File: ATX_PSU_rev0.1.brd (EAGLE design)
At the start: 160 x 100 mm, 60 parts, among them J1 ATX24RH, U1 INA169, U2 INA169, U3 INA169, U4 INA169, U5 INA169

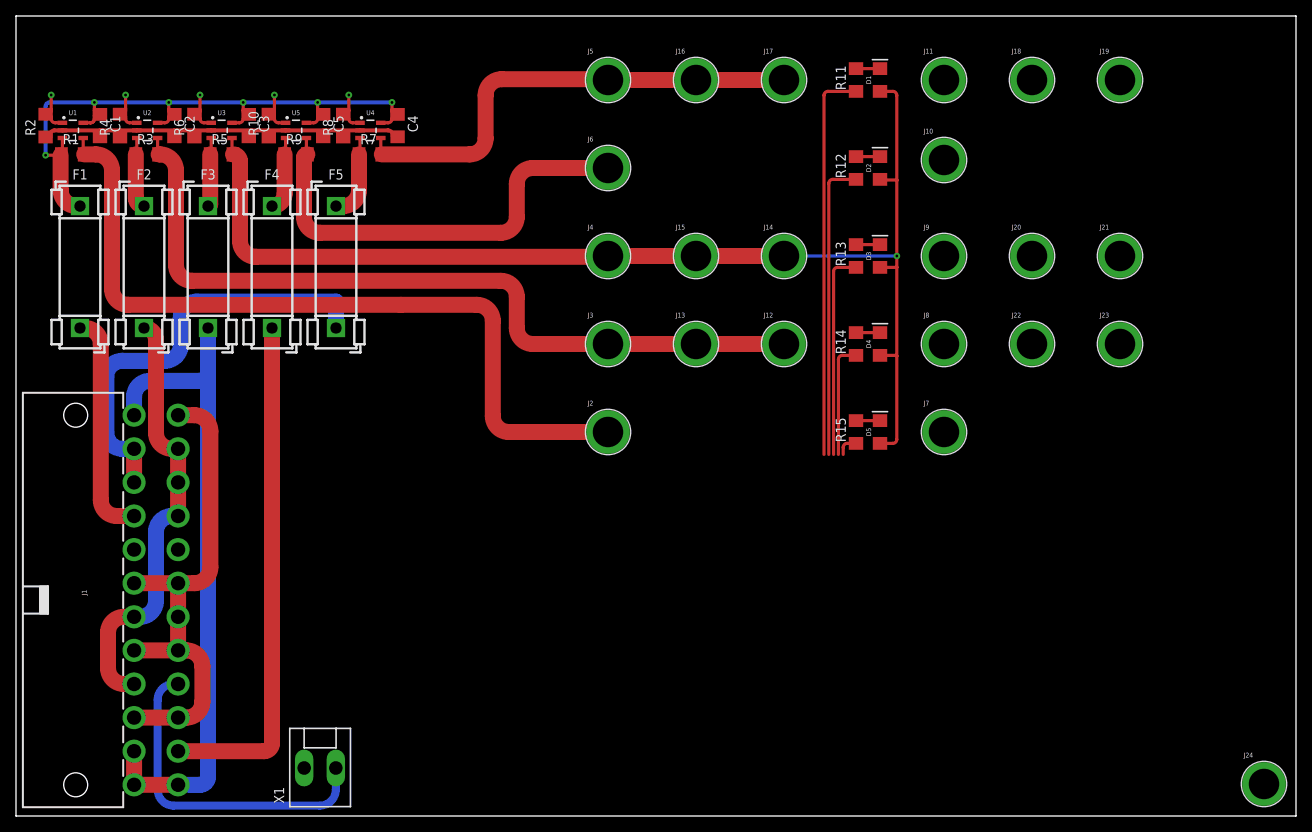
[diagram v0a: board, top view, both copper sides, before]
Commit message: added microcontroller
made some connections to microcontroller.
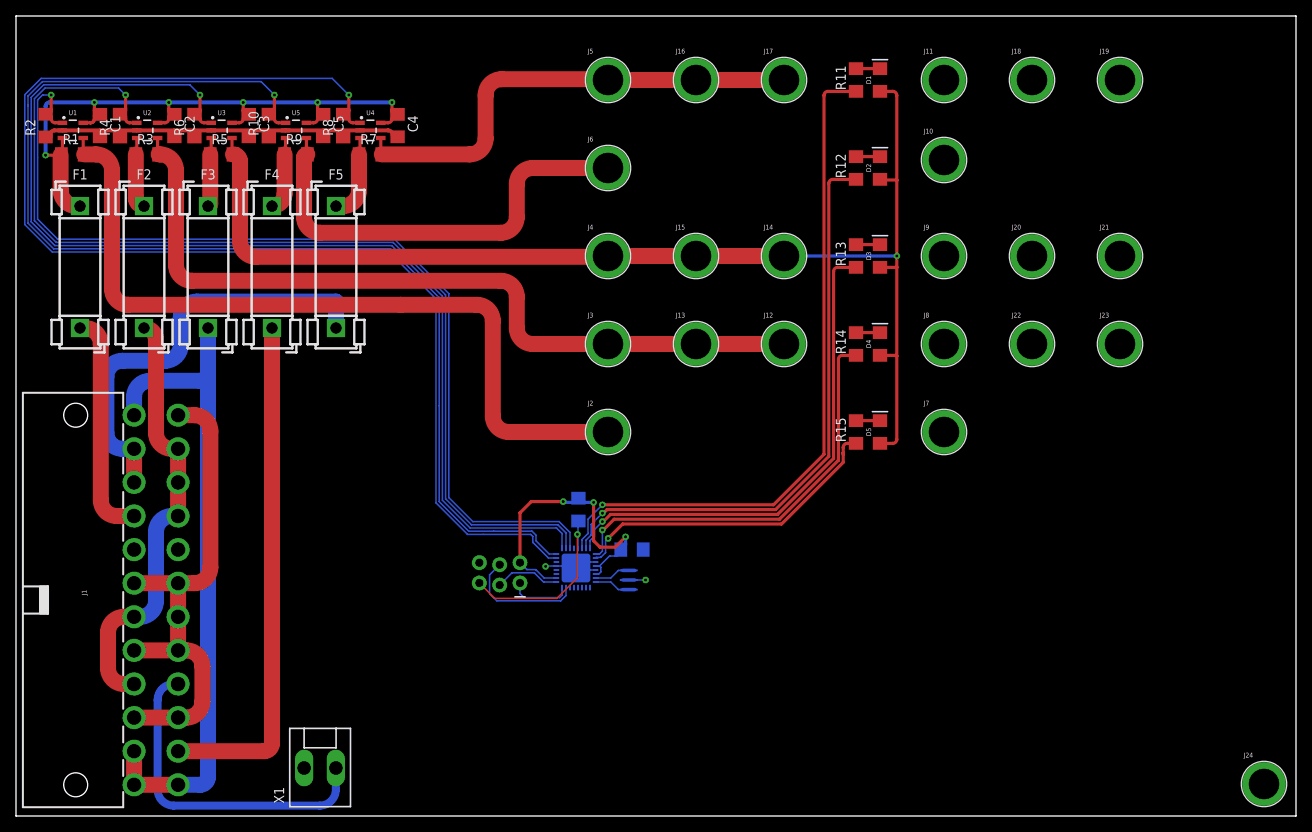
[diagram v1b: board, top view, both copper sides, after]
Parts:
- added C6: 100nF, resistor:C1206
- added J25: AVR_SPI_PROG_3X22X3_LOCK, SparkFun-Connectors:2X3_LOCK
- added R16: 10K, resistor:R1206
- added U7: (no value), Seeed-IC:QFN32G-0.5-5X5MM
- added Y1: (no value), SparkFun-Clocks:RESONATOR-SMD-3.2X1.3
- C1, C2, C3, C4, C5: value (none) -> 0.1uF
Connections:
- removed net N$10: R14.1
- removed net N$12: R13.1
- removed net N$13: R12.1
- removed net N$14: R11.1
- removed net N$9: R15.1
- new net LED0: R11.1, U7.30
- new net LED1: R12.1, U7.31
- new net LED2: R13.1, U7.32
- new net LED3: R14.1, U7.1
- new net LED4: R15.1, U7.2
- new net MISO: J25.1, U7.16
- new net MOSI: J25.4, U7.15
- new net N$11: U7.7, Y1.3
- new net N$8: U7.8, Y1.1
- new net RST: J25.5, R16.1, U7.29
- new net SCK: J25.3, U7.17
- net 5V_STDBY_PRE: now also C6.1, J25.2, R16.2, U7.18, U7.4, U7.6
- net ECHO_0: now also U7.27
- net ECHO_1: now also U7.26
- net ECHO_2: now also U7.25
- net ECHO_3: now also U7.23
- net ECHO_4: now also U7.24
- net GND: now also C6.2, J25.6, U7.21, U7.3, U7.33, U7.5, Y1.2
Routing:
- net ECHO_3: track 5.49 -> 163.0 mm
- net ECHO_4: track 5.49 -> 152.3 mm
- net ECHO_2: track 5.49 -> 142.6 mm
- net ECHO_1: track 5.50 -> 132.5 mm
- net ECHO_0: track 5.50 -> 122.1 mm
- net LED0: track 0.00 -> 85.9 mm, vias 0 -> 1
- net LED1: track 0.00 -> 74.2 mm, vias 0 -> 1
- net LED2: track 0.00 -> 62.5 mm, vias 0 -> 1
- net LED3: track 0.00 -> 51.8 mm, vias 0 -> 1
- net N$14: track 49.1 -> 0.00 mm
- net LED4: track 0.00 -> 40.6 mm, vias 0 -> 1
- net 5V_STDBY_PRE: track 85.7 -> 125.1 mm, vias 6 -> 9
- net N$13: track 37.5 -> 0.00 mm
- net N$12: track 25.9 -> 0.00 mm
- net RST: track 0.00 -> 23.1 mm, vias 0 -> 1
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
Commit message: added some parts
LCD with I2C backpack and 3 buttons.
I belive routing is finished, but I want to reroute using polygons for large connectors, and figure out how this will be enclosed.
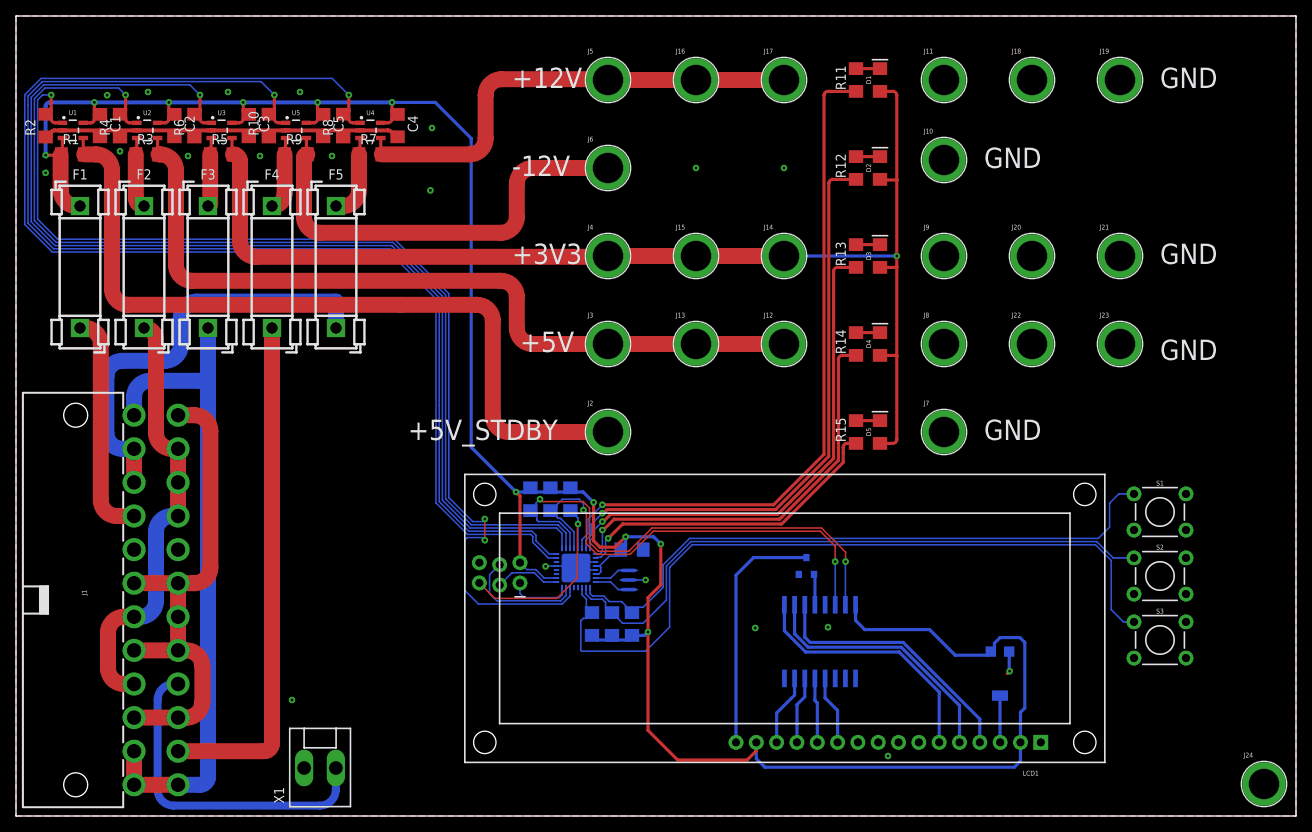
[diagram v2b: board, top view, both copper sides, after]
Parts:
- added IC1: PCF8574T, micro-philips:SO16W
- added LCD1: LCD-16X2SILK, SparkFun-Displays:LCD-16X2
- added Q1: 600mA/40V, SparkFun-DiscreteSemi:SOT23-3
- added R17, R18: 4.7K, resistor:R1206
- added R19: (no value), resistor:RTRIM3314G
- added R20, R21, R22: 10K, resistor:R1206
- added S1, S2, S3: MOMENTARY-SWITCH-SPST-PTH-6.0MM, SparkFun-Switches:TACTILE_SWITCH_PTH_6.0MM
- moved R16 1.64 mm to (69.3, 39.6)
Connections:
- new net BUTTON0: R20.1, S1.1, U7.9
- new net BUTTON1: R21.1, S2.1, U7.10
- new net BUTTON2: R22.1, S3.1, U7.11
- new net N$10: IC1.7, LCD1.14
- new net N$12: IC1.9, LCD1.6
- new net N$13: IC1.10, LCD1.5
- new net N$14: IC1.11, LCD1.4
- new net N$15: IC1.12, Q1.1
- new net N$16: LCD1.16, Q1.3
- new net N$18: LCD1.3, R19.2
- new net N$3: IC1.4, LCD1.11
- new net N$7: IC1.5, LCD1.12
- new net N$9: IC1.6, LCD1.13
- new net SCL: IC1.14, R18.1, U7.28
- new net SDA: IC1.15, R17.1, U7.27
- net 5V_STDBY_PRE: now also IC1.16, LCD1.15, LCD1.2, R17.2, R18.2, R19.3, R20.2, R21.2, R22.2
- net ECHO_0: now also U7.14; no longer U7.27
- net GND: now also IC1.1, IC1.2, IC1.3, IC1.8, LCD1.1, Q1.2, R19.1, S1.3, S2.3, S3.3
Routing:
- net 5V_STDBY_PRE: track 125.1 -> 318.1 mm, vias 9 -> 11
- net BUTTON2: track 0.00 -> 96.3 mm
- net BUTTON0: track 0.00 -> 79.6 mm
- net BUTTON1: track 0.00 -> 78.9 mm
- net SDA: track 0.00 -> 63.0 mm, vias 0 -> 2
- net SCL: track 0.00 -> 57.6 mm, vias 0 -> 2
- net N$14: track 0.00 -> 33.1 mm
- net N$13: track 0.00 -> 32.6 mm
- net N$12: track 0.00 -> 32.1 mm
- net N$16: track 0.00 -> 30.6 mm
- net ECHO_0: track 122.1 -> 136.2 mm, vias 1 -> 3
- net N$10: track 0.00 -> 8.93 mm
- net N$3: track 0.00 -> 8.65 mm
- net N$9: track 0.00 -> 8.40 mm
- net N$7: track 0.00 -> 8.12 mm
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- added copper zone on layer 1, net GND
- added copper zone on layer 16, net GND
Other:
- board text added: "+12V"
- board text added: "+3V3"
- board text added: "+5V"
- board text added: "+5V_STDBY"
- board text added: "-12V"
- board text added: "GND"
